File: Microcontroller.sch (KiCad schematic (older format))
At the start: 41 parts, among them CN2 CONN_RCPT_USB2.0_MINI_B_SMD_R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, M1 2N7002BK, M2 2N7002BK, Q10 2N7002BK, U2 STM32L412R8T6, X1 ABM3B-16.000MHZ

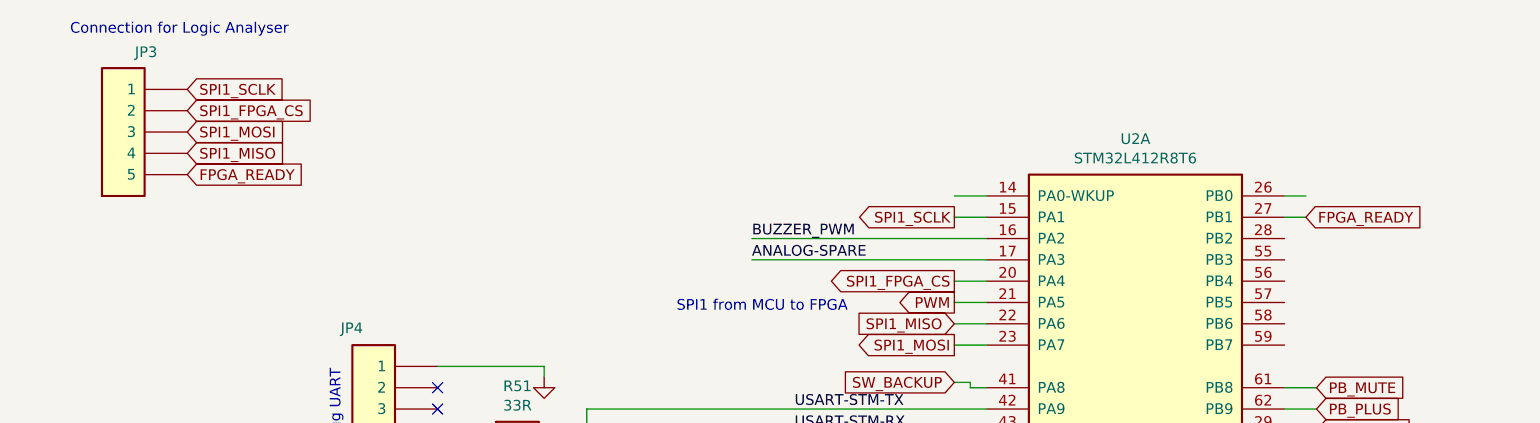
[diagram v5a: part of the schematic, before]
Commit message: JTAG pins have added
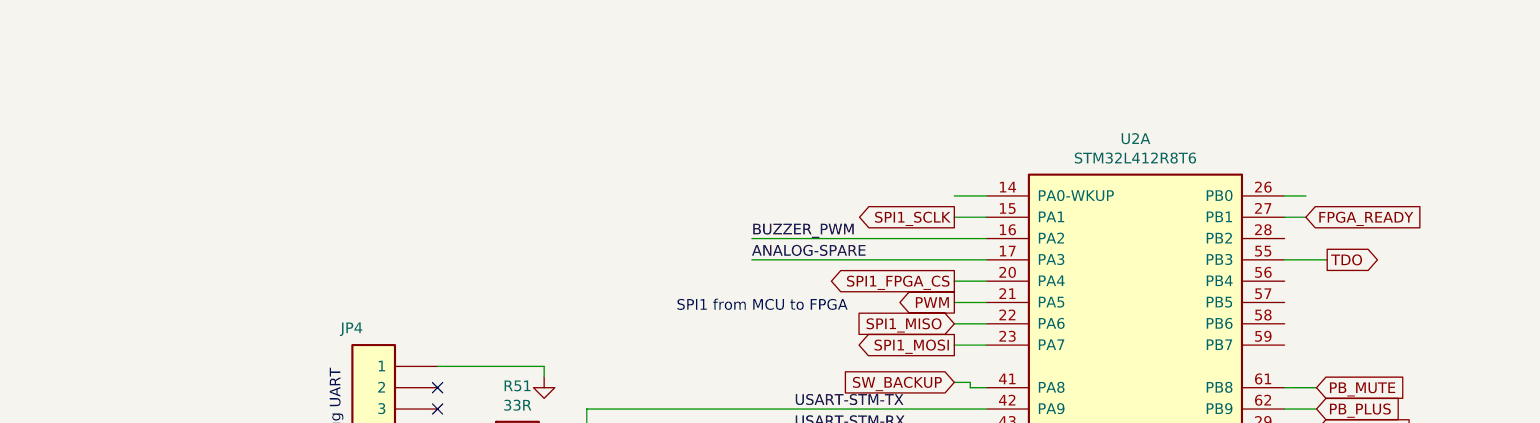
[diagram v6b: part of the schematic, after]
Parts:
- removed JP3: Pin_Header,_1x5-Way,_2.54mm_Pitch, symbol OpenVent:Pin_Header,_1x5-Way,_2.54mm_Pitch
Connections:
- net labels added: TDO
- wire segments 182 -> 183
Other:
- note removed: "Connection for Logic Analyser"
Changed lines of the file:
@@
 Text GLabel 4800 2200 0    50   Input ~ 0
 SPI1_MISO
-$Comp
-L OpenVent:Pin_Header,_1x5-Way,_2.54mm_Pitch JP3
-U 1 1 6063147A
-P 1200 1500
-F 0 "JP3" H 1393 2075 50  0000 C CNN
-F 1 "Pin_Header,_1x5-Way,_2.54mm_Pitch" H 1400 1900 50  0001 C CNN
-F 2 "" H 1400 1900 50  0001 C CNN
-F 3 "" H 1400 1900 50  0001 C CNN
-	1    1200 1500
-	-1   0    0    -1
-$EndComp
-Text Notes 650  850  0    50   ~ 0
-Connection for Logic Analyser
-Text GLabel 1200 1100 2    50   Input ~ 0
-SPI1_SCLK
-Text GLabel 1200 1200 2    50   Input ~ 0
-SPI1_FPGA_CS
-Text GLabel 1200 1300 2    50   Input ~ 0
-SPI1_MOSI
-Text GLabel 1200 1400 2    50   Input ~ 0
-SPI1_MISO
-Text GLabel 1200 1500 2    50   Input ~ 0
-FPGA_READY
+Text GLabel 6550 1900 2    50   Output ~ 0
+TDO
+Wire Wire Line
+	6350 1900 6550 1900
 $EndSCHEMATC

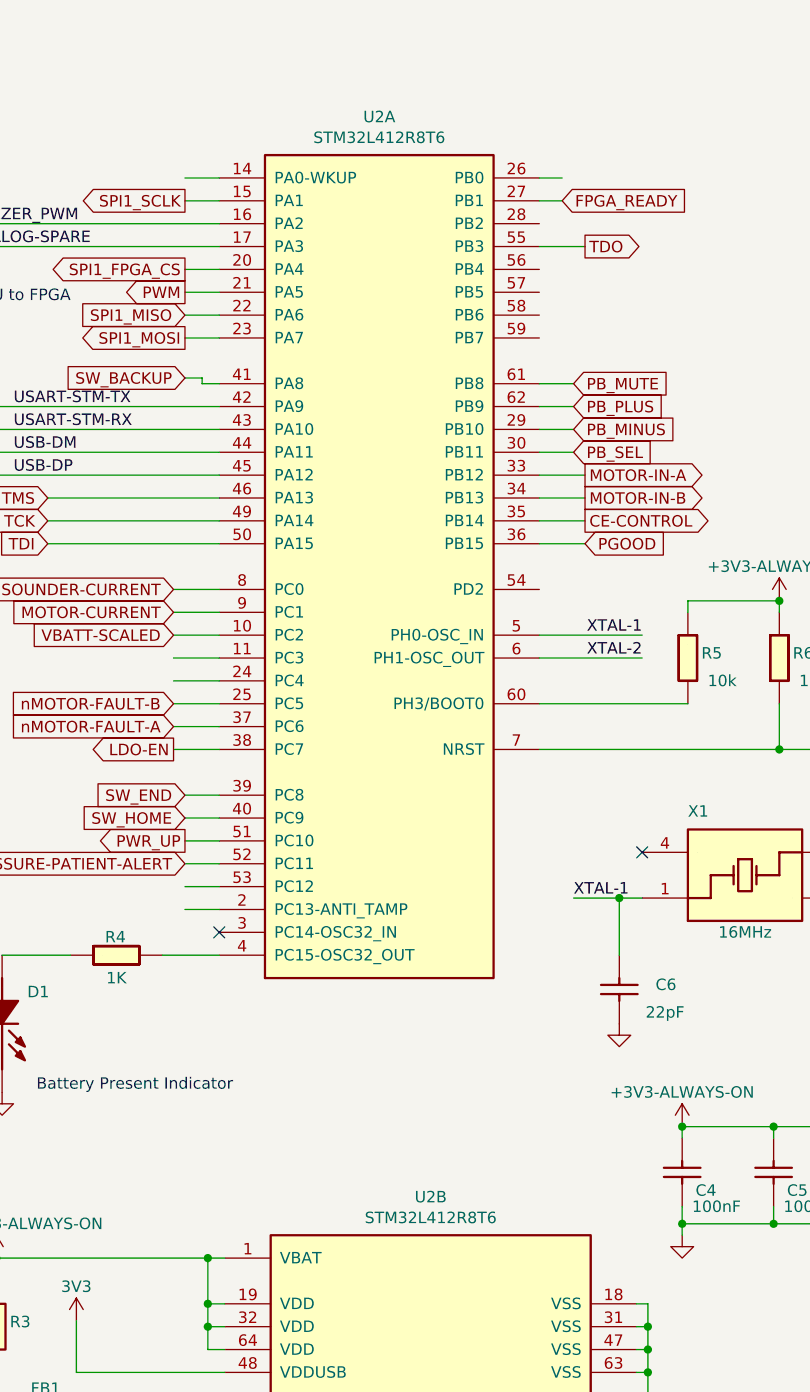
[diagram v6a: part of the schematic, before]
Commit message: STM32L476RG LQFP64
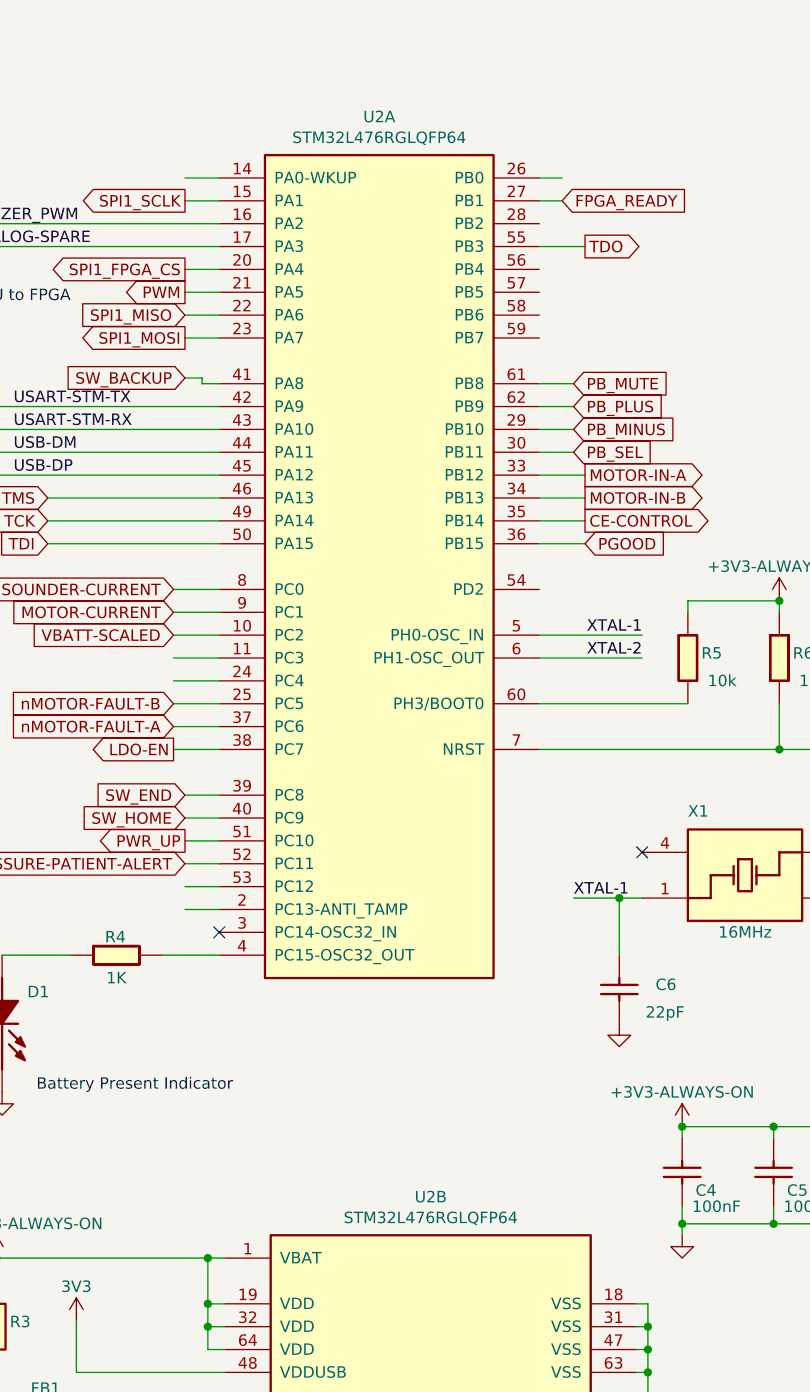
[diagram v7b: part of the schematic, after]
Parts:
- U2: value STM32L412R8T6 -> STM32L476RGLQFP64
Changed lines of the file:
@@
 P 4950 5000
 F 0 "U2" H 5650 8667 50  0000 C CNN
-F 1 "STM32L412R8T6" H 5650 8576 50  0000 C CNN
+F 1 "STM32L476RGLQFP64" H 5650 8576 50  0000 C CNN
 F 2 "Package_QFP:LQFP-64_10x10mm_P0.5mm" H 4950 5000 50  0001 C CNN
 F 3 "https://www.st.com/resource/en/datasheet/stm32l412c8.pdf" H 4950 5000 50  0001 C CNN
@@
 P 4975 7025
 F 0 "U2" H 5875 7992 50  0000 C CNN
-F 1 "STM32L412R8T6" H 5875 7901 50  0000 C CNN
+F 1 "STM32L476RGLQFP64" H 5875 7901 50  0000 C CNN
 F 2 "Package_QFP:LQFP-64_10x10mm_P0.5mm" H 4975 7025 50  0001 C CNN
 F 3 "https://www.st.com/resource/en/datasheet/stm32l412c8.pdf" H 4975 7025 50  0001 C CNN

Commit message: 8-way buffer for ADC changed to 74ACT244PW second attempt
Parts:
- U2: symbol OpenVent:STM32L412R8T6 -> OpenVent-rescue:STM32L412R8T6-OpenVent
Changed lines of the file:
@@
 Connection ~ 1450 5300
 $Comp
-L OpenVent:STM32L412R8T6 U2
+L OpenVent-rescue:STM32L412R8T6-OpenVent U2
 U 1 1 5FAE2332
 P 4950 5000
+AR Path="/5FAE2332" Ref="U2"  Part="1"
+AR Path="/5F988182/5FAE2332" Ref="U2"  Part="1"
 F 0 "U2" H 5650 8667 50  0000 C CNN
 F 1 "STM32L476RGLQFP64" H 5650 8576 50  0000 C CNN
@@
 $EndComp
 $Comp
-L OpenVent:STM32L412R8T6 U2
+L OpenVent-rescue:STM32L412R8T6-OpenVent U2
 U 2 1 5FAE4E4F
 P 4975 7025
+AR Path="/5FAE4E4F" Ref="U2"  Part="2"
+AR Path="/5F988182/5FAE4E4F" Ref="U2"  Part="2"
 F 0 "U2" H 5875 7992 50  0000 C CNN
 F 1 "STM32L476RGLQFP64" H 5875 7901 50  0000 C CNN
